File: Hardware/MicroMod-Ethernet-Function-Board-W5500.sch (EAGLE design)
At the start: 89 parts, among them J1 MAGJACK-POE, J11 MICROMOD_STANDARD, Q1 220mA/50V/3.5Ω, Q5 20V/4.2A/52mΩ/1.4W, U1 EEPROM, U3 W5500, U4 3.3V, U5 POE_PSU-DP990X, Y1 25MHz

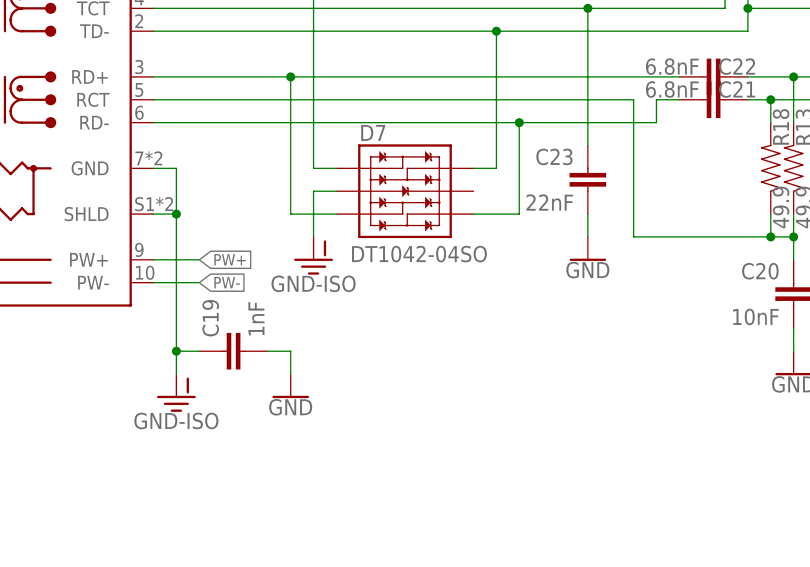
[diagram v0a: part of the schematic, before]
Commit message: Mark ESD IC as DNP
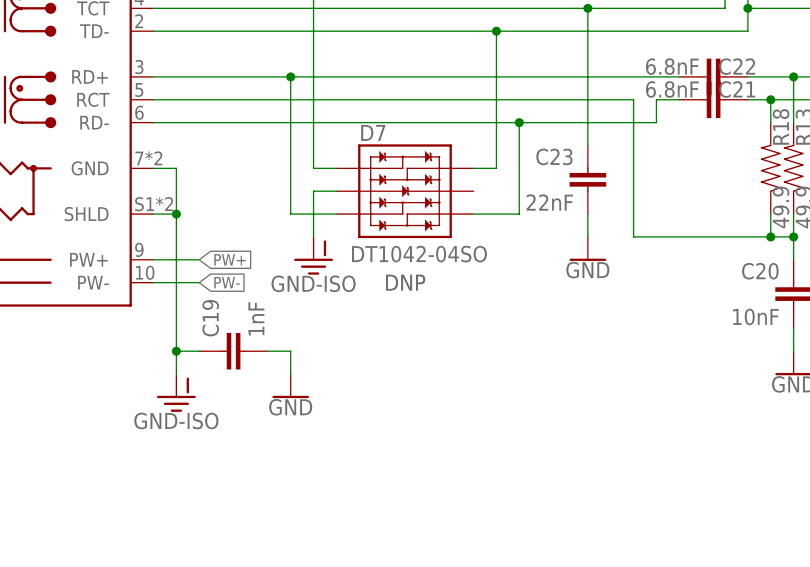
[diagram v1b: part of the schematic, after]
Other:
- note added: "DNP"
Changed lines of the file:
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@@
 <grid distance="0.1" unitdist="inch" unit="inch" style="lines" multiple="1" display="no" altdistance="0.01" altunitdist="inch" altunit="inch"/>
 <layers>
-<layer number="1" name="Top" color="4" fill="1" visible="yes" active="no"/>
-<layer number="2" name="Route2" color="1" fill="3" visible="yes" active="no"/>
-<layer number="3" name="Route3" color="4" fill="3" visible="yes" active="no"/>
-<layer number="4" name="Route4" color="1" fill="4" visible="yes" active="no"/>
-<layer number="5" name="Route5" color="4" fill="4" visible="yes" active="no"/>
-<layer number="6" name="Route6" color="1" fill="8" visible="yes" active="no"/>
-<layer number="7" name="Route7" color="4" fill="8" visible="yes" active="no"/>
-<layer number="8" name="Route8" color="1" fill="2" visible="yes" active="no"/>
-<layer number="9" name="Route9" color="4" fill="2" visible="yes" active="no"/>
-<layer number="10" name="Route10" color="1" fill="7" visible="yes" active="no"/>
-<layer number="11" name="Route11" color="4" fill="7" visible="yes" active="no"/>
-<layer number="12" name="Route12" color="1" fill="5" visible="yes" active="no"/>
-<layer number="13" name="Route13" color="4" fill="5" visible="yes" active="no"/>
-<layer number="14" name="Route14" color="1" fill="6" visible="yes" active="no"/>
-<layer number="15" name="Route15" color="4" fill="6" visible="yes" active="no"/>
-<layer number="16" name="Bottom" color="1" fill="1" visible="yes" active="no"/>
-<layer number="17" name="Pads" color="2" fill="1" visible="yes" active="no"/>
-<layer number="18" name="Vias" color="2" fill="1" visible="yes" active="no"/>
-<layer number="19" name="Unrouted" color="6" fill="1" visible="yes" active="no"/>
-<layer number="20" name="Dimension" color="24" fill="1" visible="yes" active="no"/>
-<layer number="21" name="tPlace" color="16" fill="1" visible="yes" active="no"/>
-<layer number="22" name="bPlace" color="14" fill="1" visible="yes" active="no"/>
-<layer number="23" name="tOrigins" color="15" fill="1" visible="yes" active="no"/>
-<layer number="24" name="bOrigins" color="15" fill="1" visible="yes" active="no"/>
-<layer number="25" name="tNames" color="7" fill="1" visible="yes" active="no"/>
-<layer number="26" name="bNames" color="7" fill="1" visible="yes" active="no"/>
-<layer number="27" name="tValues" color="7" fill="1" visible="yes" active="no"/>
-<layer number="28" name="bValues" color="7" fill="1" visible="yes" active="no"/>
+<layer number="1" name="Top" color="4" fill="1" visible="no" active="no"/>
+<layer number="2" name="Route2" color="1" fill="3" visible="no" active="no"/>
+<layer number="3" name="Route3" color="4" fill="3" visible="no" active="no"/>
+<layer number="4" name="Route4" color="1" fill="4" visible="no" active="no"/>
+<layer number="5" name="Route5" color="4" fill="4" visible="no" active="no"/>
+<layer number="6" name="Route6" color="1" fill="8" visible="no" active="no"/>
+<layer number="7" name="Route7" color="4" fill="8" visible="no" active="no"/>
+<layer number="8" name="Route8" color="1" fill="2" visible="no" active="no"/>
+<layer number="9" name="Route9" color="4" fill="2" visible="no" active="no"/>
+<layer number="10" name="Route10" color="1" fill="7" visible="no" active="no"/>
+<layer number="11" name="Route11" color="4" fill="7" visible="no" active="no"/>
+<layer number="12" name="Route12" color="1" fill="5" visible="no" active="no"/>
+<layer number="13" name="Route13" color="4" fill="5" visible="no" active="no"/>
+<layer number="14" name="Route14" color="1" fill="6" visible="no" active="no"/>
+<layer number="15" name="Route15" color="4" fill="6" visible="no" active="no"/>
+<layer number="16" name="Bottom" color="1" fill="1" visible="no" active="no"/>
+<layer number="17" name="Pads" color="2" fill="1" visible="no" active="no"/>
+<layer number="18" name="Vias" color="2" fill="1" visible="no" active="no"/>
+<layer number="19" name="Unrouted" color="6" fill="1" visible="no" active="no"/>
+<layer number="20" name="Dimension" color="24" fill="1" visible="no" active="no"/>
+<layer number="21" name="tPlace" color="16" fill="1" visible="no" active="no"/>
+<layer number="22" name="bPlace" color="14" fill="1" visible="no" active="no"/>
+<layer number="23" name="tOrigins" color="15" fill="1" visible="no" active="no"/>
+<layer number="24" name="bOrigins" color="15" fill="1" visible="no" active="no"/>
+<layer number="25" name="tNames" color="7" fill="1" visible="no" active="no"/>
+<layer number="26" name="bNames" color="7" fill="1" visible="no" active="no"/>
+<layer number="27" name="tValues" color="7" fill="1" visible="no" active="no"/>
+<layer number="28" name="bValues" color="7" fill="1" visible="no" active="no"/>
 <layer number="29" name="tStop" color="7" fill="3" visible="no" active="no"/>
 <layer number="30" name="bStop" color="7" fill="6" visible="no" active="no"/>
@@
 <layer number="35" name="tGlue" color="7" fill="4" visible="no" active="no"/>
 <layer number="36" name="bGlue" color="7" fill="5" visible="no" active="no"/>
-<layer number="37" name="tTest" color="7" fill="1" visible="yes" active="no"/>
-<layer number="38" name="bTest" color="7" fill="1" visible="yes" active="no"/>
+<layer number="37" name="tTest" color="7" fill="1" visible="no" active="no"/>
+<layer number="38" name="bTest" color="7" fill="1" visible="no" active="no"/>
 <layer number="39" name="tKeepout" color="4" fill="11" visible="no" active="no"/>
 <layer number="40" name="bKeepout" color="1" fill="11" visible="no" active="no"/>
@@
 <layer number="44" name="Drills" color="7" fill="1" visible="no" active="no"/>
 <layer number="45" name="Holes" color="7" fill="1" visible="no" active="no"/>
-<layer number="46" name="Milling" color="3" fill="1" visible="yes" active="no"/>
-<layer number="47" name="Measures" color="7" fill="1" visible="yes" active="no"/>
-<layer number="48" name="Document" color="7" fill="1" visible="yes" active="no"/>
-<layer number="49" name="Reference" color="7" fill="1" visible="yes" active="no"/>
-<layer number="50" name="dxf" color="7" fill="1" visible="yes" active="no"/>
-<layer number="51" name="tDocu" color="6" fill="1" visible="yes" active="no"/>
-<layer number="52" name="bDocu" color="7" fill="1" visible="yes" active="no"/>
-<layer number="53" name="tGND_GNDA" color="7" fill="9" visible="yes" active="no"/>
-<layer number="54" name="bGND_GNDA" color="1" fill="9" visible="yes" active="no"/>
-<layer number="56" name="wert" color="7" fill="1" visible="yes" active="no"/>
-<layer number="57" name="tCAD" color="7" fill="1" visible="yes" active="no"/>
-<layer number="58" name="bCAD" color="7" fill="1" visible="yes" active="no"/>
-<layer number="59" name="tCarbon" color="7" fill="1" visible="yes" active="no"/>
-<layer number="60" name="bCarbon" color="7" fill="1" visible="yes" active="no"/>
+<layer number="46" name="Milling" color="3" fill="1" visible="no" active="no"/>
+<layer number="47" name="Measures" color="7" fill="1" visible="no" active="no"/>
+<layer number="48" name="Document" color="7" fill="1" visible="no" active="no"/>
+<layer number="49" name="Reference" color="7" fill="1" visible="no" active="no"/>
+<layer number="50" name="dxf" color="7" fill="1" visible="no" active="no"/>
+<layer number="51" name="tDocu" color="6" fill="1" visible="no" active="no"/>
+<layer number="52" name="bDocu" color="7" fill="1" visible="no" active="no"/>
+<layer number="53" name="tGND_GNDA" color="7" fill="9" visible="no" active="no"/>
+<layer number="54" name="bGND_GNDA" color="1" fill="9" visible="no" active="no"/>
+<layer number="56" name="wert" color="7" fill="1" visible="no" active="no"/>
+<layer number="57" name="tCAD" color="7" fill="1" visible="no" active="no"/>
+<layer number="58" name="bCAD" color="7" fill="1" visible="no" active="no"/>
+<layer number="59" name="tCarbon" color="7" fill="1" visible="no" active="no"/>
+<layer number="60" name="bCarbon" color="7" fill="1" visible="no" active="no"/>
 <layer number="88" name="SimResults" color="9" fill="1" visible="yes" active="yes"/>
 <layer number="89" name="SimProbes" color="9" fill="1" visible="yes" active="yes"/>
@@
 <wire x1="337.82" y1="137.16" x2="337.82" y2="279.4" width="0.2032" layer="97" style="longdash"/>
 <text x="236.22" y="71.12" size="1.778" layer="97" font="vector" align="center">Dummy Load: 100mA</text>
+<text x="269.24" y="193.04" size="1.778" layer="97" font="vector" align="center">DNP</text>
 </plain>
 <instances>
